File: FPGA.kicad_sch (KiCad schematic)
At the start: 121 parts, among them U3A1 LFE5U-25F-8MG285C, U3B1 LFE5U-25F-8MG285C, U3C1 LFE5U-25F-8MG285C, U3D1 LFE5U-25F-8MG285C, U3E1 LFE5U-25F-8MG285C, U3F1 LFE5U-25F-8MG285C, U3G1 LFE5U-25F-8MG285C, U7 CAT24C128, U8 W25Q128JVP

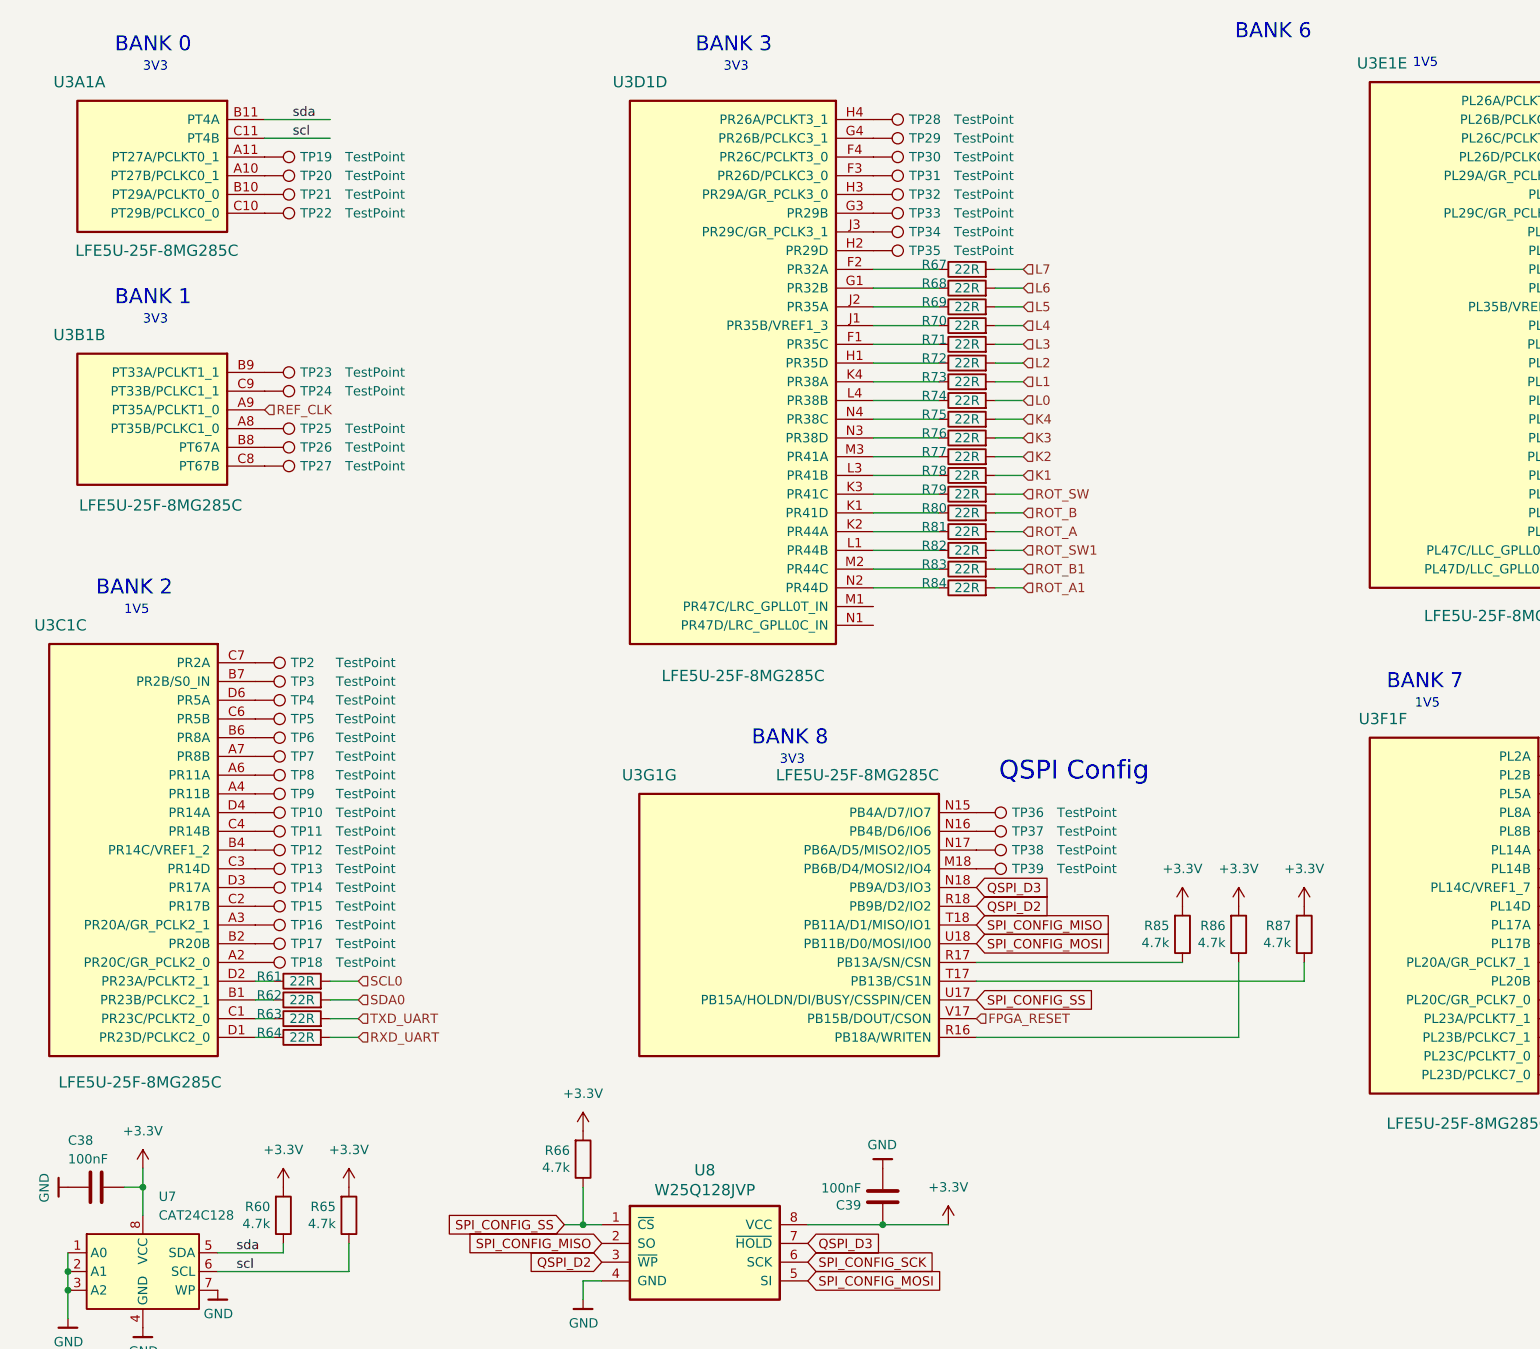
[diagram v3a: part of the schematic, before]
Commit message: Assign jlcpcb pn. Fix footprint assign, uniform resistor value for battery charger
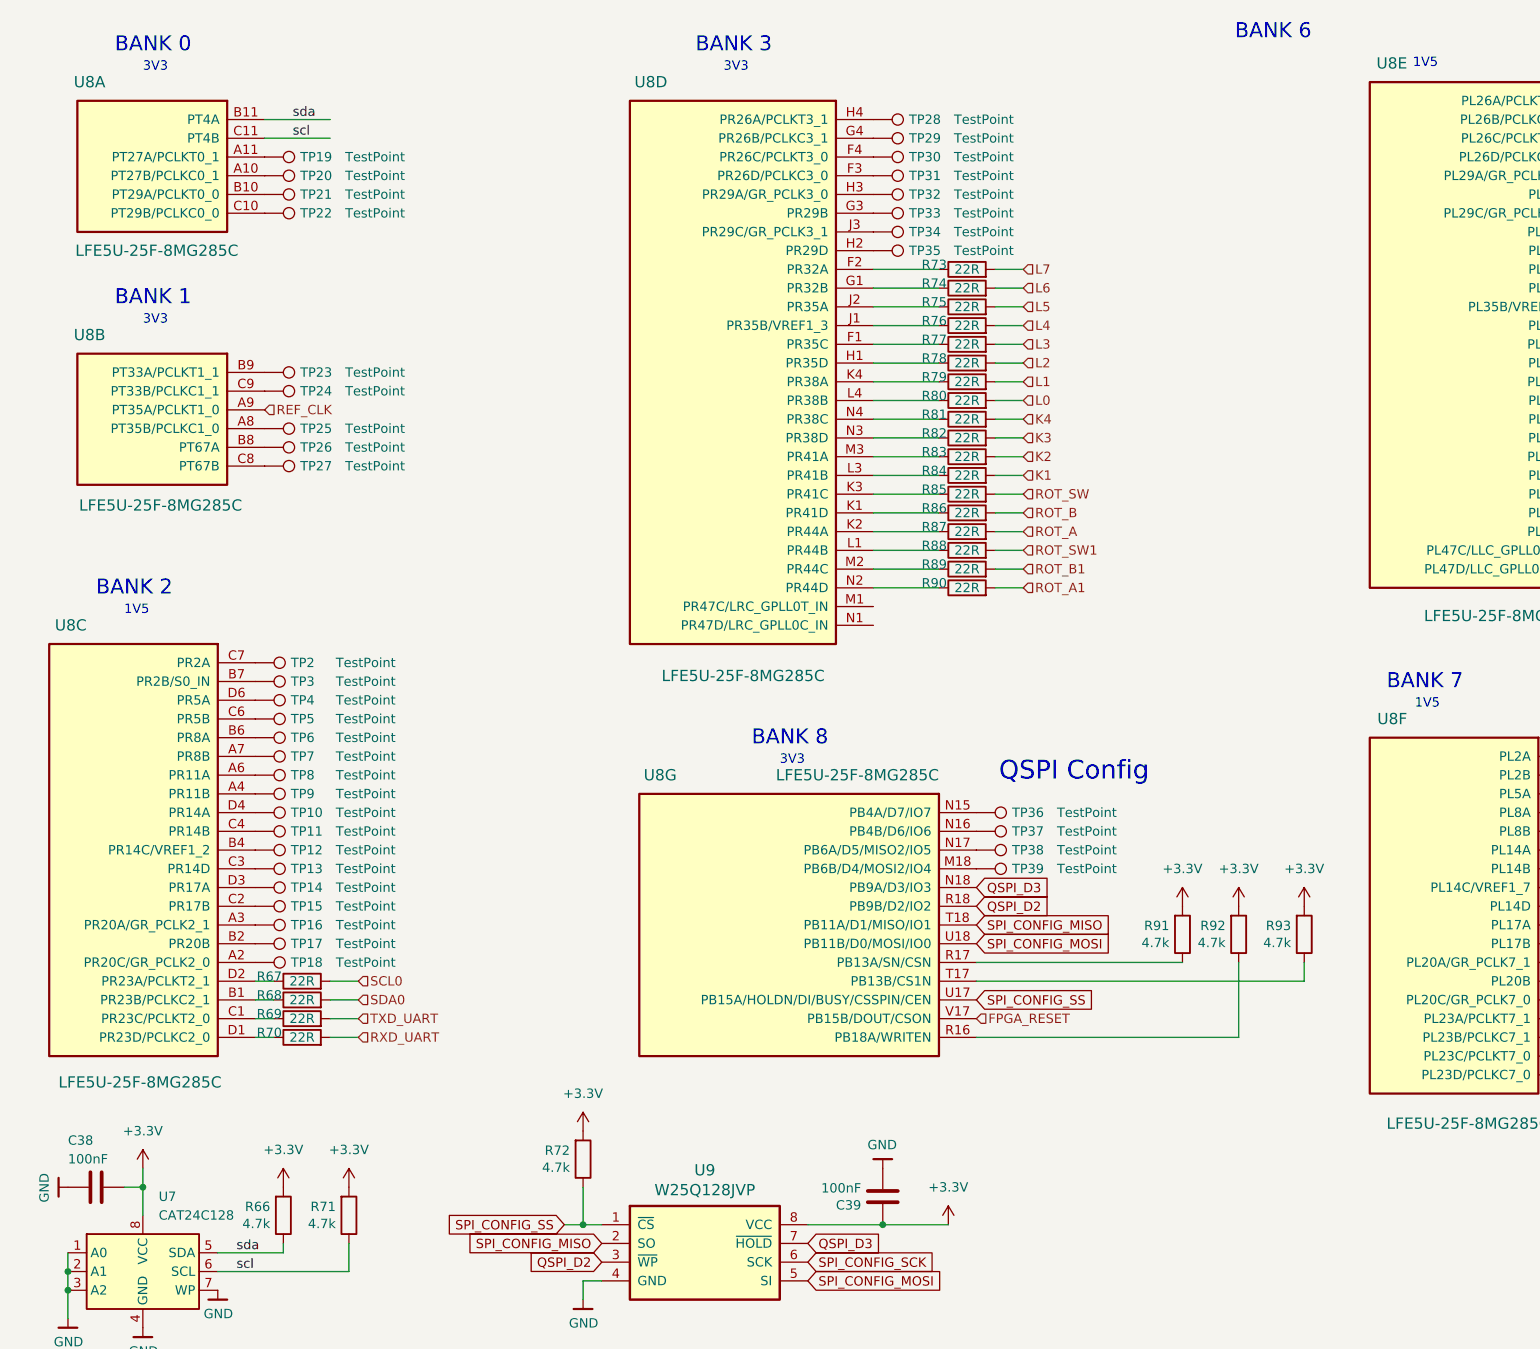
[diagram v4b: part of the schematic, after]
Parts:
- U8: renamed from U3A1; footprint gkl_housings_bga:csBGA285 -> kicad:BGA-285
- U8: renamed from U3B1; footprint gkl_housings_bga:csBGA285 -> kicad:BGA-285
- U8: renamed from U3C1; footprint gkl_housings_bga:csBGA285 -> kicad:BGA-285
- U8: renamed from U3D1; footprint gkl_housings_bga:csBGA285 -> kicad:BGA-285
- U8: renamed from U3E1; footprint gkl_housings_bga:csBGA285 -> kicad:BGA-285
- U8: renamed from U3F1; footprint gkl_housings_bga:csBGA285 -> kicad:BGA-285
- U8: renamed from U3G1; footprint gkl_housings_bga:csBGA285 -> kicad:BGA-285
- renumbered R60 to R66, R61 to R67, R62 to R68, R63 to R69, R64 to R70, R65 to R71, R66 to R72, R67 to R73, R68 to R74, R69 to R75, R70 to R76, R71 to R77, R72 to R78, R73 to R79, R74 to R80, R75 to R81, R76 to R82, R77 to R83, R78 to R84, R79 to R85, R80 to R86, R81 to R87, R82 to R88, R83 to R89, R84 to R90, R85 to R91, R86 to R92, R87 to R93, U8 to U9
